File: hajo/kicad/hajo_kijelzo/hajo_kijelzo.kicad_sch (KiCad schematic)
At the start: 26 parts, among them J1 Seetalk NG, J2 Batteries, J3 Terminator, J4 Conn_01x14, Q1 BC557, U1 MCP2562, U2 LF50CV, U3 LF33_TO220

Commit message: fix boards
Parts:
- Q1: footprint Package_TO_SOT_THT:TO-92_Inline -> Package_TO_SOT_THT:TO-92_Inline_Wide
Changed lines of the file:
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@@
       (effects (font (size 1.27 1.27)) (justify left))
     )
-    (property "Footprint" "Package_TO_SOT_THT:TO-92_Inline" (at 247.65 125.095 0)
+    (property "Footprint" "Package_TO_SOT_THT:TO-92_Inline_Wide" (at 247.65 125.095 0)
       (effects (font (size 1.27 1.27) italic) (justify left) hide)
     )

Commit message: display pcb add capacitor, change R values
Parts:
- added C6: 2.2u, Capacitor_THT:CP_Radial_D5.0mm_P2.00mm, symbol Device:C_Polarized
- R1, R3, R5: value 200 -> 51.1
- R2, R4, R6: value 16.9K -> 806
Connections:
- net +3.3V: now also C6.1
- net GND: now also C6.2
- no-connect marks 21 -> 20
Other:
- moved on the sheet: C4, U3

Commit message: pcb changes
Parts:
- C1, C3, C5: footprint Capacitor_THT:C_Rect_L7.0mm_W2.0mm_P5.00mm -> Capacitor_THT:C_Rect_L4.0mm_W2.5mm_P2.50mm
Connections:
- net DRV2: now also A1.6 (GPIO4/ADC1_3); no longer A1.5 (GPIO3/ADC1_2)
- net DRV3: now also A1.9 (GPIO7/ADC1_6); no longer A1.7 (GPIO5/ADC1_4)
- net ADC3_H: now reaches A1.10 (GPIO8/ADC1_7)
- net ADC3_H: now also J2.2 (Pin_2), R6.2
- net ADC3_L: now reaches A1.11 (GPIO9/ADC1_8)
- net ADC3_L: now also C5.2, J2.1 (Pin_1), R5.2
- net ADC2_H: now reaches J2.4 (Pin_4), R4.2
- net ADC2_H: now also A1.7 (GPIO5/ADC1_4)
- net ADC1_H: now reaches J2.6 (Pin_6), R2.2
- net ADC1_H: now also A1.4 (GPIO2/ADC1_1)
- net ADC1 renamed ADC1_L
- net ADC1_L: now also A1.5 (GPIO3/ADC1_2); no longer A1.4 (GPIO2/ADC1_1)
- net ADC2 renamed ADC2_L
- net ADC2_L: now also A1.8 (GPIO6/ADC1_5); no longer A1.6 (GPIO4/ADC1_3)
- removed net ADC3: A1.8 (GPIO6/ADC1_5), C5.2, J2.1 (Pin_1), R5.2
- no-connect marks 20 -> 17
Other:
- moved on the sheet: C3, C5, R2, R3, R4, R5, R6

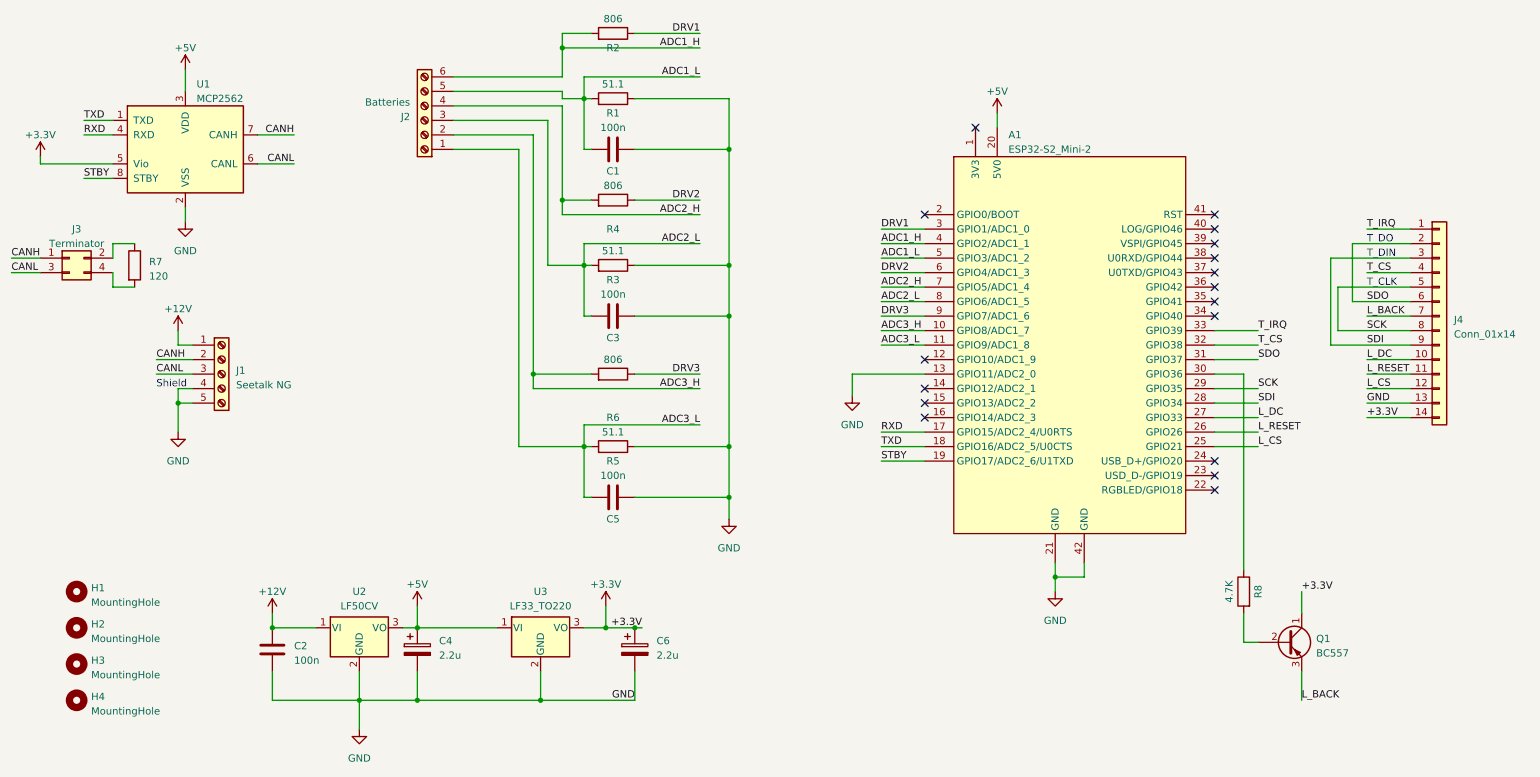
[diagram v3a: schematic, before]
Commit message: kijelzo on new board
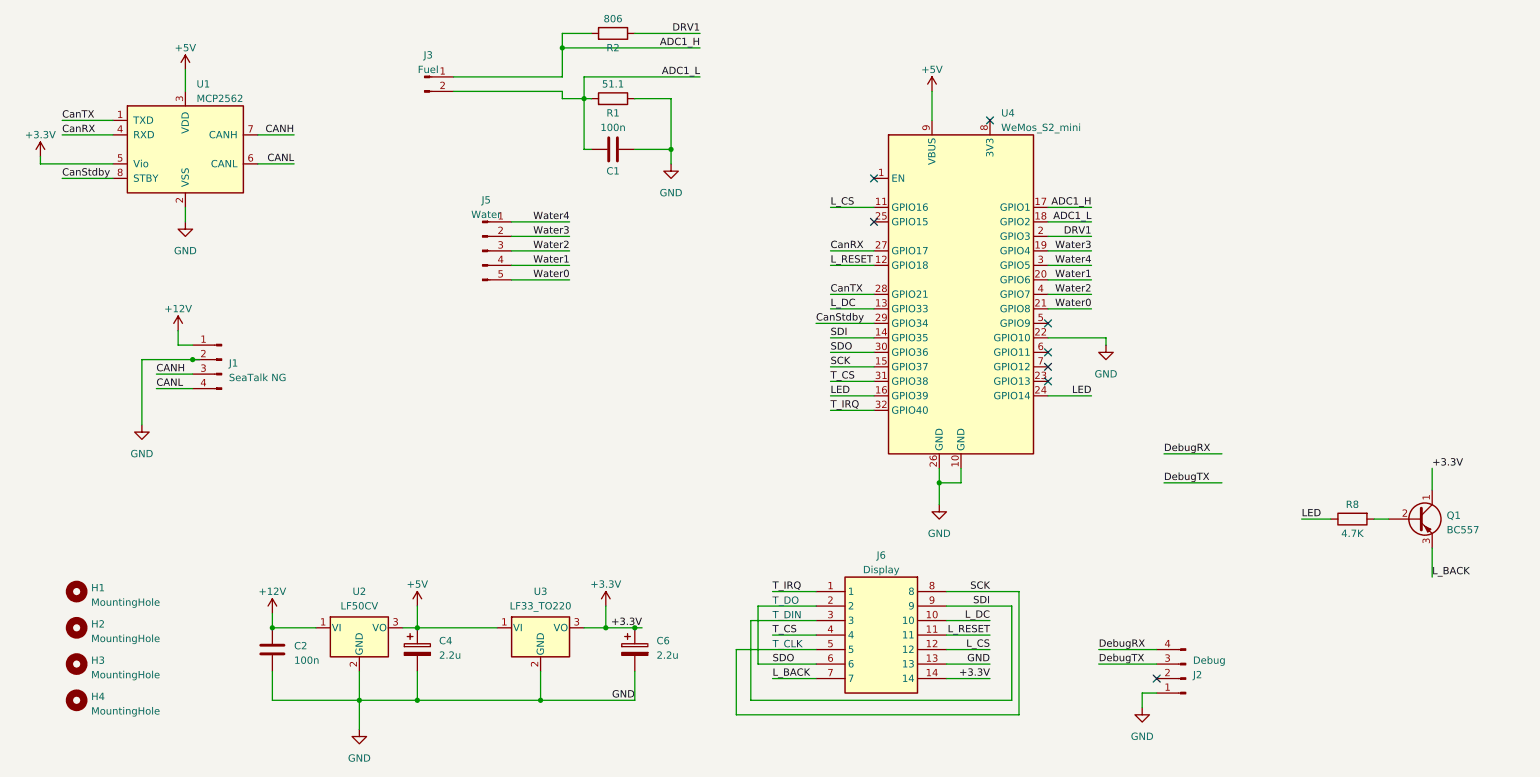
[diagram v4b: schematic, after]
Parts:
- removed A1: ESP32-S2_Mini-2, own:DIP-42_W15.24mm, symbol own:ESP32-S2_Mini-2
- removed C3, C5: 100n, Capacitor_THT:C_Rect_L4.0mm_W2.5mm_P2.50mm, symbol Device:C
- removed J1: Seetalk NG, Connector_Phoenix_MC_HighVoltage:PhoenixContact_MCV_1,5_5-G-5.08_1x05_P5.08mm_Vertical, symbol Connector:Screw_Terminal_01x05
- removed J2: Batteries, Connector_Phoenix_MC_HighVoltage:PhoenixContact_MCV_1,5_6-G-5.08_1x06_P5.08mm_Vertical, symbol Connector:Screw_Terminal_01x06
- removed J3: Terminator, Connector_PinHeader_2.54mm:PinHeader_2x02_P2.54mm_Vertical, symbol Connector_Generic:Conn_02x02_Odd_Even
- removed J4: Conn_01x14, Connector_PinHeader_2.54mm:PinHeader_1x14_P2.54mm_Vertical, symbol Connector_Generic:Conn_01x14
- removed R3, R5: 51.1, Resistor_THT:R_Axial_DIN0207_L6.3mm_D2.5mm_P7.62mm_Horizontal, symbol Device:R
- removed R4, R6: 806, Resistor_THT:R_Axial_DIN0207_L6.3mm_D2.5mm_P7.62mm_Horizontal, symbol Device:R
- removed R7: 120, Resistor_THT:R_Axial_DIN0207_L6.3mm_D2.5mm_P7.62mm_Horizontal, symbol Device:R
- added J1: SeaTalk NG, Connector_PinHeader_2.54mm:PinHeader_1x04_P2.54mm_Vertical, symbol Connector:Conn_01x04_Pin
- added J2: Debug, Connector_PinHeader_2.54mm:PinHeader_1x04_P2.54mm_Vertical, symbol Connector:Conn_01x04_Pin
- added J3: Fuel, SamacSys_Parts:1821245, symbol Connector:Conn_01x02_Pin
- added J5: Water, SamacSys_Parts:1821274, symbol Connector:Conn_01x05_Pin
- added J6: Display, 1844772, symbol SamacSys_Parts:1844772
- added U4: WeMos_S2_mini, own:WEMOS_S2_mini_traced, symbol own:WeMos_S2_mini
- U2, U3: footprint Package_TO_SOT_THT:TO-220-3_Horizontal_TabDown -> Package_TO_SOT_THT:TO-220-3_Vertical
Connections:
- net +12V: now also J1.1 (Pin_1)
- net +3.3V: now also J6.14
- net +5V: now also U4.9 (VBUS)
- net ADC1_H: now also J3.1 (Pin_1), U4.17 (GPIO1)
- net ADC1_L: now also J3.2 (Pin_2), U4.18 (GPIO2)
- net CANH: now also J1.3 (Pin_3)
- net CANL: now also J1.4 (Pin_4)
- net DRV1: now also U4.2 (GPIO3)
- net GND: now also J1.2 (Pin_2), J2.1 (Pin_1), J6.13, U4.10 (GND), U4.22 (GPIO10), U4.26 (GND)
- net L_BACK: now also J6.7
- net L_CS: now also J6.12, U4.11 (GPIO16)
- net L_DC: now also J6.10, U4.13 (GPIO33)
- net L_RESET: now also J6.11, U4.12 (GPIO18)
- net SCK: now also J6.5, J6.8, U4.15 (GPIO37)
- net SDI: now also J6.3, J6.9, U4.14 (GPIO35)
- net SDO: now also J6.2, J6.6, U4.30 (GPIO36)
- net T_CS: now also J6.4, U4.31 (GPIO38)
- net T_IRQ: now also J6.1, U4.32 (GPIO40)
- net LED: now reaches R8.1
- net LED: now also U4.16 (GPIO39), U4.24 (GPIO14)
- net RXD renamed CanRX
- net CanRX: now also U4.27 (GPIO17)
- net STBY renamed CanStdby
- net CanStdby: now also U4.29 (GPIO34)
- net TXD renamed CanTX
- net CanTX: now also U4.28 (GPIO21)
- new net DebugRX: J2.4 (Pin_4)
- new net DebugTX: J2.3 (Pin_3)
- new net Water0: J5.5 (Pin_5), U4.21 (GPIO8)
- new net Water1: J5.4 (Pin_4), U4.20 (GPIO6)
- new net Water2: J5.3 (Pin_3), U4.4 (GPIO7)
- new net Water3: J5.2 (Pin_2), U4.19 (GPIO4)
- new net Water4: J5.1 (Pin_1), U4.3 (GPIO5)
- no-connect marks 17 -> 8
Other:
- note removed: "Shield"
- moved on the sheet: Q1, R8

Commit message: pcv rework
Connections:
- net ADC1_H: now also U4.3 (GPIO5); no longer U4.17 (GPIO1)
- net ADC1_L: now also U4.4 (GPIO7); no longer U4.18 (GPIO2)
- net CanRX: now also U4.11 (GPIO16); no longer U4.27 (GPIO17)
- net CanTX: now also U4.27 (GPIO17); no longer U4.28 (GPIO21)
- net DebugRX: now also J2.3 (Pin_3), U4.32 (GPIO40); no longer J2.4 (Pin_4)
- net DebugTX: now also J2.4 (Pin_4), U4.16 (GPIO39); no longer J2.3 (Pin_3)
- net GND: now also U1.8 (STBY), U4.18 (GPIO2); no longer U4.22 (GPIO10)
- net LED: now also U4.23 (GPIO13); no longer U4.16 (GPIO39), U4.24 (GPIO14)
- net L_CS: now also U4.28 (GPIO21); no longer U4.11 (GPIO16)
- net L_DC: now also U4.30 (GPIO36); no longer U4.13 (GPIO33)
- net L_RESET: now also U4.29 (GPIO34); no longer U4.12 (GPIO18)
- net SCK: now also U4.12 (GPIO18); no longer U4.15 (GPIO37)
- net SDO: now also U4.15 (GPIO37); no longer U4.30 (GPIO36)
- net T_CS: now also U4.13 (GPIO33); no longer U4.31 (GPIO38)
- net T_IRQ: now also U4.31 (GPIO38); no longer U4.32 (GPIO40)
- net Water0: now also U4.7 (GPIO12); no longer U4.21 (GPIO8)
- net Water1: now also U4.6 (GPIO11); no longer U4.20 (GPIO6)
- net Water2: now also U4.21 (GPIO8); no longer U4.4 (GPIO7)
- net Water3: now also U4.5 (GPIO9); no longer U4.19 (GPIO4)
- net Water4: now also U4.20 (GPIO6); no longer U4.3 (GPIO5)
- removed net CanStdby: U1.8 (STBY), U4.29 (GPIO34)

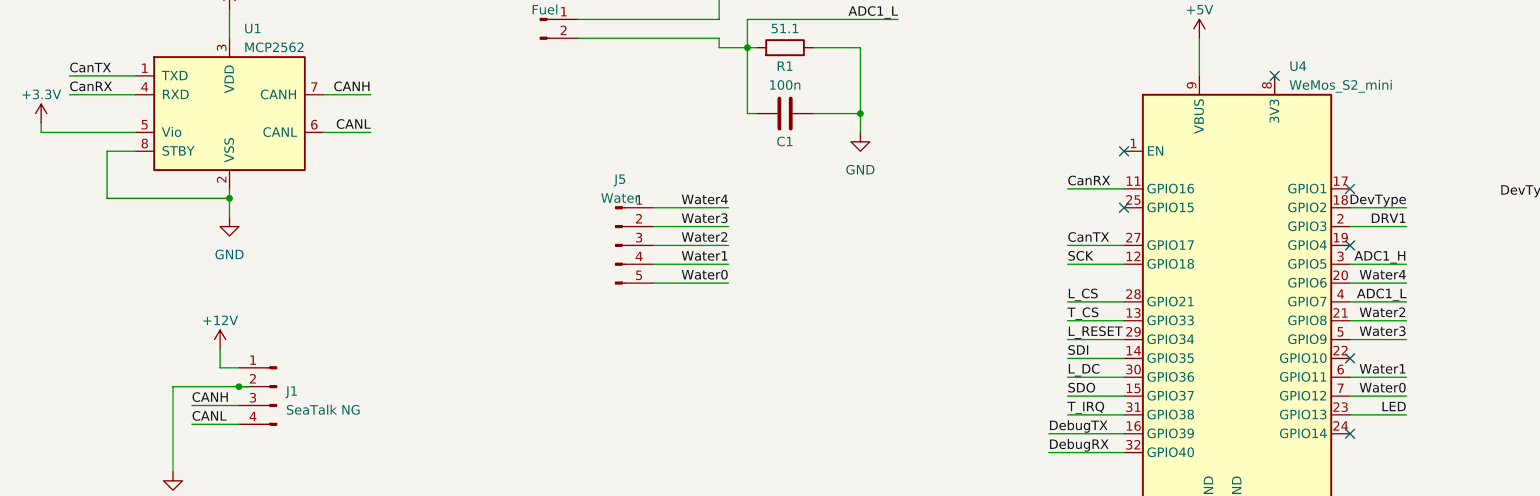
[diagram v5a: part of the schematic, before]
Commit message: add back CanStby
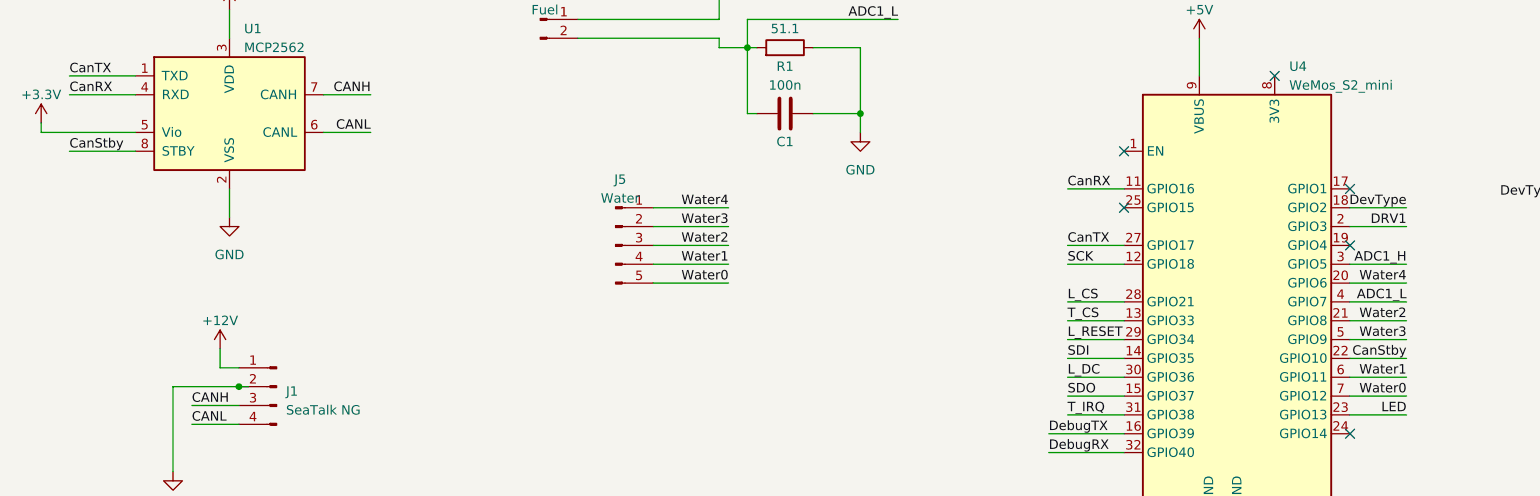
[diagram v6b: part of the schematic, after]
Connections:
- net GND: no longer U1.8 (STBY)
- net CanStby: now reaches U4.22 (GPIO10)
- net CanStby: now also U1.8 (STBY)
- no-connect marks 8 -> 7
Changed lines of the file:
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@@
 (kicad_sch (version 20230121) (generator eeschema)
   (paper "A4")
-  (junction (at 49.53 48.26) (diameter 0) (color 0 0 0 0)
-  )
   (junction (at 111.76 133.35) (diameter 0) (color 0 0 0 0)
   )
@@
   (junction (at 123.19 120.65) (diameter 0) (color 0 0 0 0)
   )
-  (no_connect (at 200.66 69.85))
   (no_connect (at 190.5 31.75))
   (no_connect (at 200.66 54.61))
@@
     (stroke (width 0) (type default))
   )
-  (wire (pts (xy 49.53 46.99) (xy 49.53 48.26))
+  (wire (pts (xy 49.53 46.99) (xy 49.53 50.8))
     (stroke (width 0) (type default))
   )
@@
     (stroke (width 0) (type default))
   )
+  (wire (pts (xy 200.66 69.85) (xy 208.28 69.85))
+    (stroke (width 0) (type default))
+  )
   (wire (pts (xy 41.91 73.66) (xy 41.91 85.09))
     (stroke (width 0) (type default))
   )
-  (wire (pts (xy 33.02 41.91) (xy 33.02 48.26))
-    (stroke (width 0) (type default))
-  )
   (wire (pts (xy 120.65 16.51) (xy 115.57 16.51))
     (stroke (width 0) (type default))
@@
     (stroke (width 0) (type default))
   )
+  (wire (pts (xy 27.94 41.91) (xy 36.83 41.91))
+    (stroke (width 0) (type default))
+  )
   (wire (pts (xy 87.63 120.65) (xy 90.17 120.65))
     (stroke (width 0) (type default))
   )
-  (wire (pts (xy 33.02 48.26) (xy 49.53 48.26))
-    (stroke (width 0) (type default))
-  )
   (wire (pts (xy 115.57 19.05) (xy 115.57 24.13))
     (stroke (width 0) (type default))
@@
     (stroke (width 0) (type default))
   )
-  (wire (pts (xy 36.83 41.91) (xy 33.02 41.91))
-    (stroke (width 0) (type default))
-  )
   (wire (pts (xy 200.66 64.77) (xy 208.28 64.77))
     (stroke (width 0) (type default))
@@
     (stroke (width 0) (type default))
   )
-  (wire (pts (xy 49.53 48.26) (xy 49.53 50.8))
-    (stroke (width 0) (type default))
-  )
   (wire (pts (xy 200.66 57.15) (xy 208.28 57.15))
     (stroke (width 0) (type default))
@@
     (effects (font (size 1.27 1.27)) (justify right bottom))
   )
+  (label "CanStby" (at 27.94 41.91 0) (fields_autoplaced)
+    (effects (font (size 1.27 1.27)) (justify left bottom))
+  )
   (label "Water4" (at 116.84 49.53 180) (fields_autoplaced)
     (effects (font (size 1.27 1.27)) (justify right bottom))
@@
     (effects (font (size 1.27 1.27)) (justify left bottom))
   )
+  (label "CanStby" (at 208.28 69.85 180) (fields_autoplaced)
+    (effects (font (size 1.27 1.27)) (justify right bottom))
+  )
   (label "DevType" (at 228.6 48.26 180) (fields_autoplaced)

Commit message: amend & upgrade pcbs
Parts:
- added R3: 10K, Resistor_THT:R_Axial_DIN0207_L6.3mm_D2.5mm_P7.62mm_Horizontal, symbol Device:R
- Q1: footprint Package_TO_SOT_THT:TO-92_Inline_Wide -> Package_TO_SOT_THT:TO-92_Inline
- U1: footprint Package_DIP:DIP-8_W7.62mm_Socket -> Package_DIP:DIP-8_W7.62mm
- U4: footprint own:WEMOS_S2_mini_traced -> own:WEMOS_S2_mini
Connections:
- net GND: now also J2.2 (Pin_2), R3.2
- net at Q1.2 (B), R8.2: now also R3.1
- no-connect marks 7 -> 6
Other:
- moved on the sheet: R8

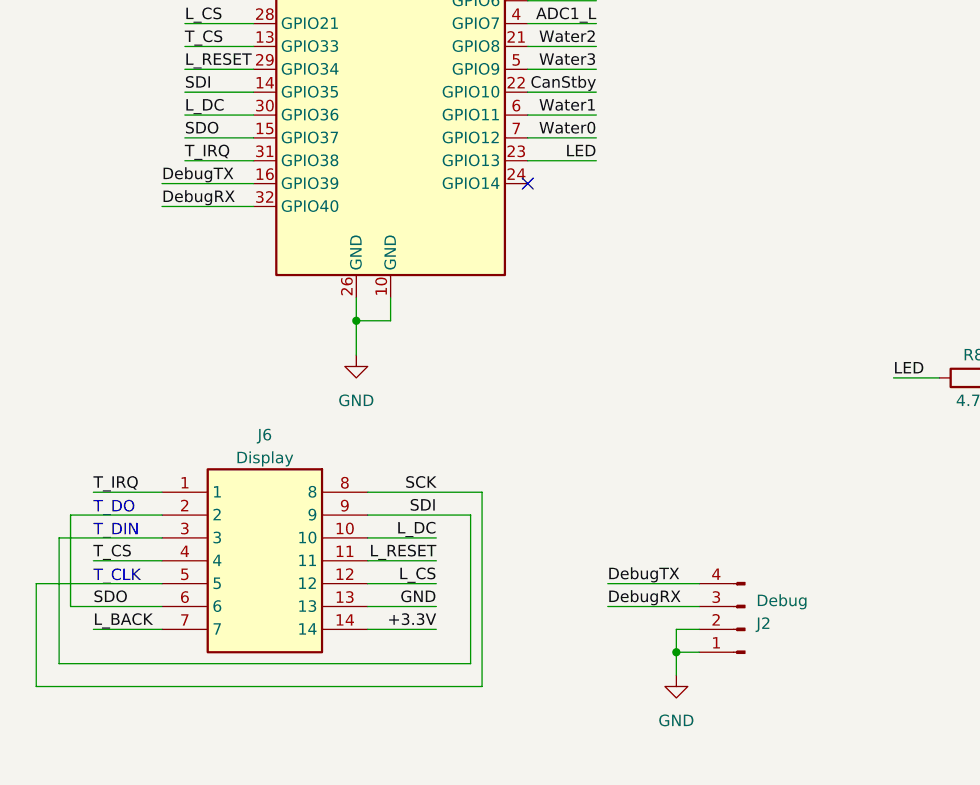
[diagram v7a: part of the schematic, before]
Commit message: update existing pcbs
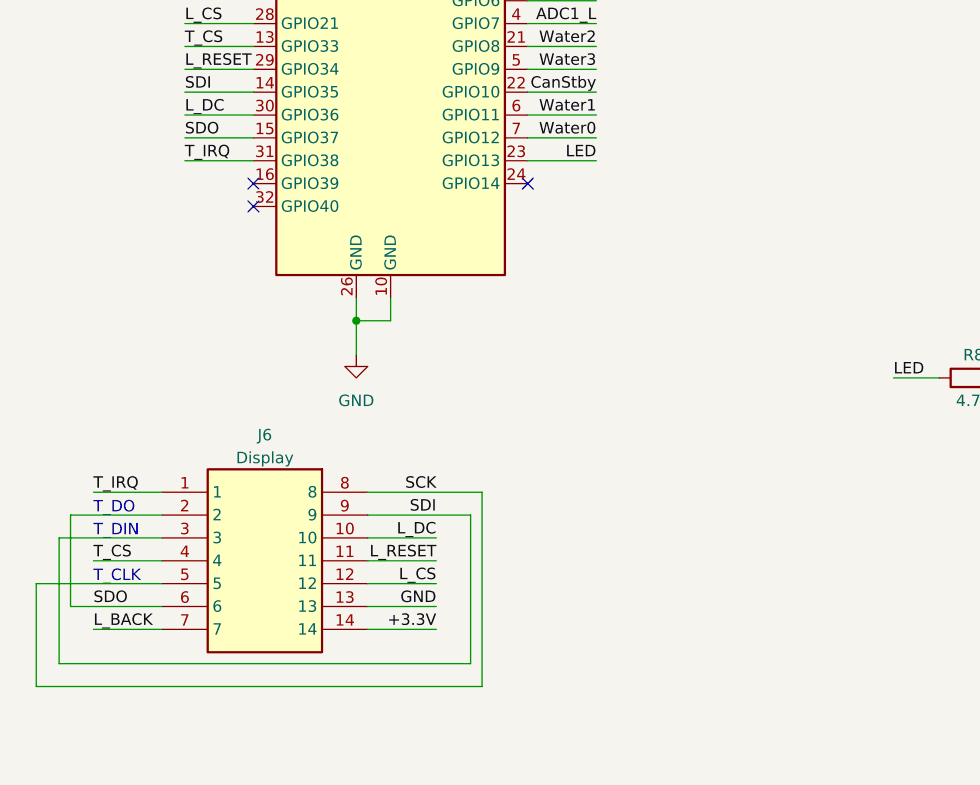
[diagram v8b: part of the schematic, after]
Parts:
- removed J2: Debug, Connector_PinHeader_2.54mm:PinHeader_1x04_P2.54mm_Vertical, symbol Connector:Conn_01x04_Pin
- J1: footprint Connector_PinHeader_2.54mm:PinHeader_1x04_P2.54mm_Vertical -> Connector_JST:JST_XH_B4B-XH-A_1x04_P2.50mm_Vertical
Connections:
- net DebugRX: no longer names the net of U4.32 (GPIO40)
- net DebugTX: no longer names the net of U4.16 (GPIO39)
- no-connect marks 6 -> 8
